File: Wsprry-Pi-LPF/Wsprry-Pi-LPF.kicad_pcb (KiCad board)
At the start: 2 copper layers, 36.8 x 12.9 mm, 13 parts, among them J1 Conn_01x04, J2 Conn_01x04

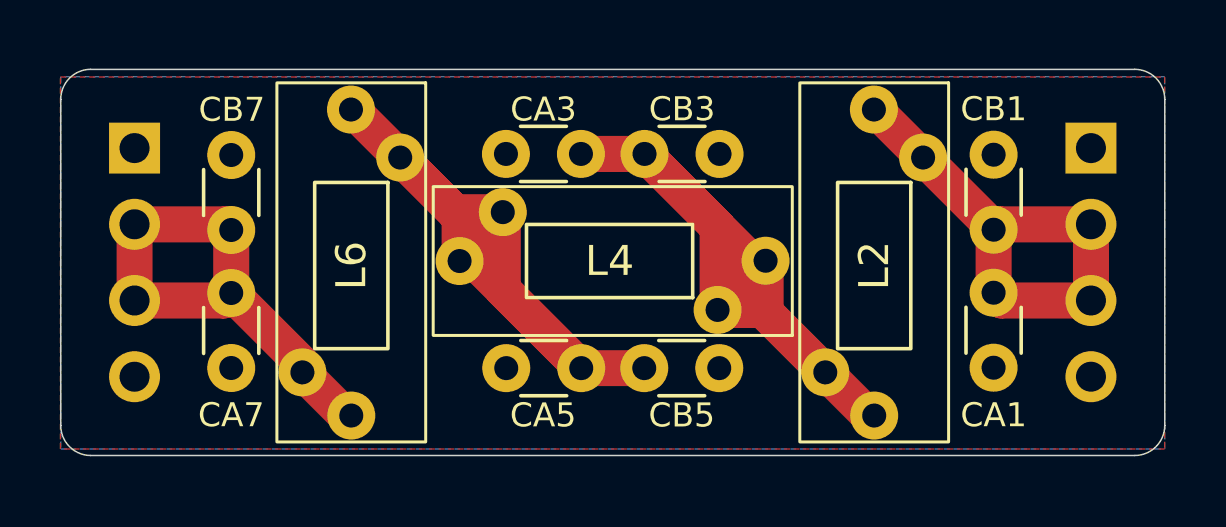
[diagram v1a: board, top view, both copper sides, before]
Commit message: Header changed to match QRP Labs
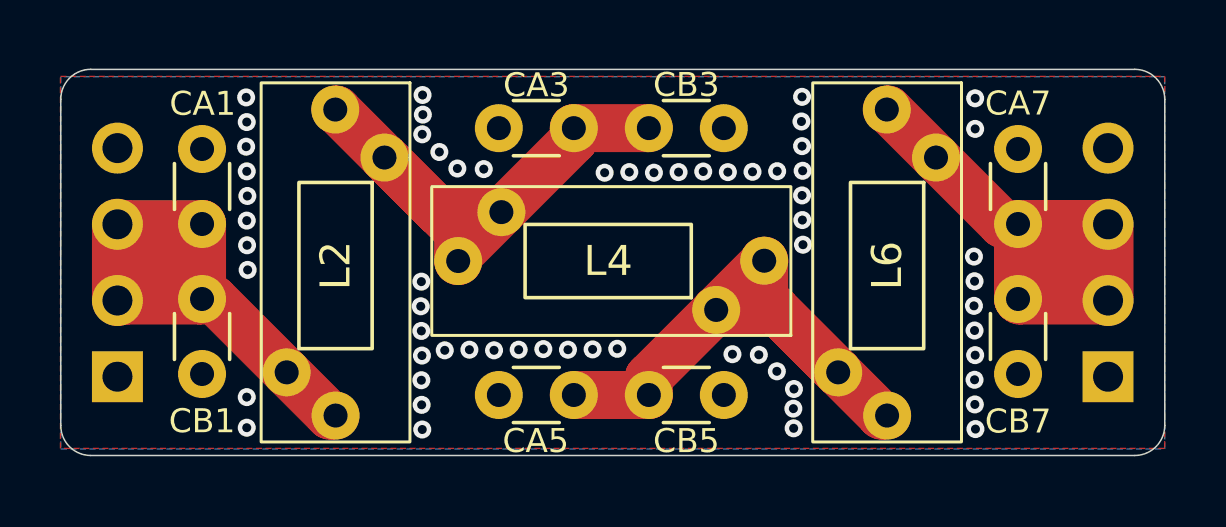
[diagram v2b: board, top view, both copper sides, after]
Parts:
- removed J2: Conn_01x04, Wsprry Pi LPF:PinHeader_1x04_P2.54mm_Vertical
- J1: value Conn_01x04 -> Jumper Pair; footprint Wsprry Pi LPF:PinHeader_1x04_P2.54mm_Vertical -> Wsprry Pi LPF:LPF_HeaderPair_2x1x04_P2.54mm_S33.02mm
- moved J1 33.3 mm to (120.5, 102.9), turned to 0 degrees
- moved CA1 0.99 mm to (123.3, 95.3)
- moved CB1 0.99 mm to (123.3, 102.8)
- moved CA5 0.93 mm to (133.2, 103.5)
- moved CB5 0.91 mm to (140.7, 103.5)
- moved CA3 0.89 mm to (133.2, 94.6)
- moved CB3 0.87 mm to (140.7, 94.6)
- moved CB7 0.84 mm to (150.5, 102.8)
- moved CA7 0.84 mm to (150.5, 95.3)
- moved L2 0.52 mm to (127.7, 99.2)
- moved L6 0.43 mm to (146.1, 99.2)
- renumbered CB7 to CA1, CB1 to CA7, CA7 to CB1, CA1 to CB7, L6 to L2, L2 to L6
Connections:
- CA1 pad 2: /RF_OUT -> /RF_IN
- CA7 pad 2: /RF_IN -> /RF_OUT
- CB1 pad 2: /RF_OUT -> /RF_IN
- CB7 pad 2: /RF_IN -> /RF_OUT
- L2 pad 1: Net-(CA5-Pad2) -> Net-(CA3-Pad2)
- L2 pad 2: /RF_OUT -> /RF_IN
- L4 pad 1: Net-(CA3-Pad2) -> Net-(CA5-Pad2)
- L4 pad 2: Net-(CA5-Pad2) -> Net-(CA3-Pad2)
- L6 pad 1: /RF_IN -> /RF_OUT
- L6 pad 2: Net-(CA3-Pad2) -> Net-(CA5-Pad2)
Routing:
- net /RF_OUT: track 17.1 -> 25.1 mm
- net /RF_IN: track 17.0 -> 24.5 mm
- net Net-(CA3-Pad2): track 27.4 -> 19.9 mm
- net Net-(CA5-Pad2): track 26.9 -> 20.5 mm
- net GND: vias 0 -> 62
